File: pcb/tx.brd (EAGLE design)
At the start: 28 x 37 mm, 54 parts, among them U3 MCP73831T-2ACI/OT, Y1 CRYSTAL-26MHZSMD-3.2X2.5

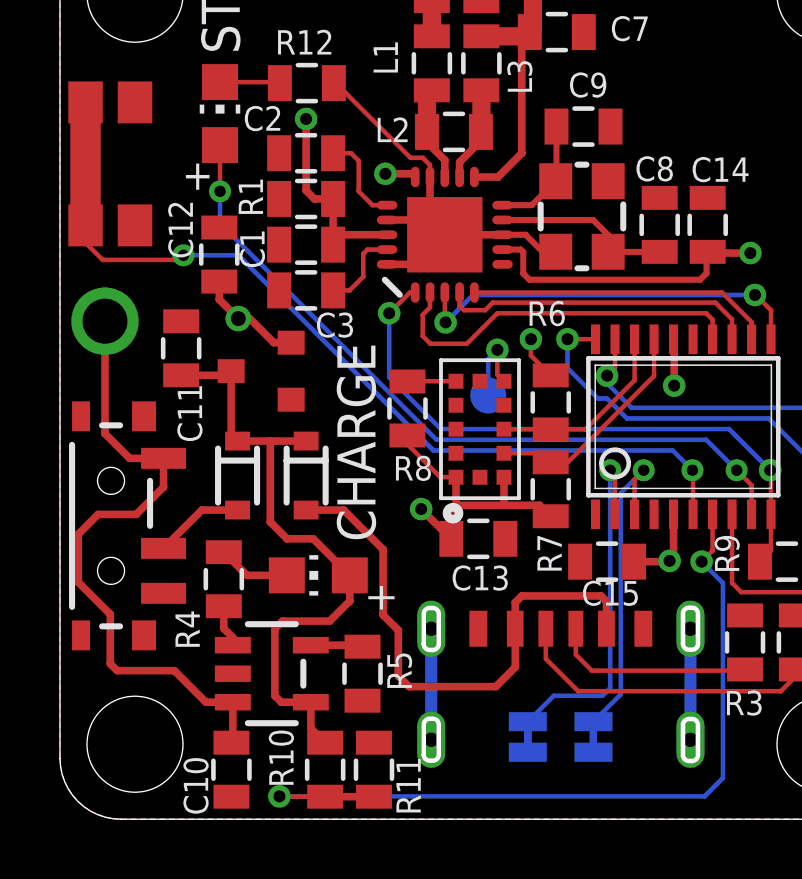
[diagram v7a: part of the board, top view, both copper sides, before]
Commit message: switched rx to tssop20
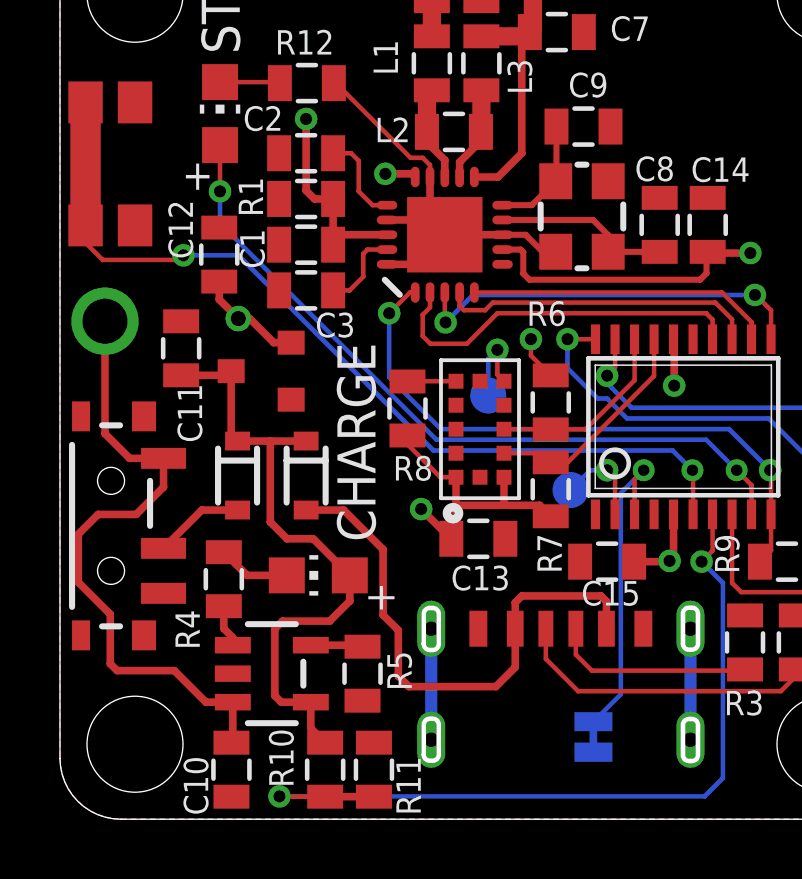
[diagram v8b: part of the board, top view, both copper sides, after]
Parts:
- removed SJ1: JUMPER-SMT_2_NC_TRACE_NO-SILK, SparkFun-Jumpers:SMT-JUMPER_2_NC_TRACE_NO-SILK
- added TP2: TPTP12R, testpad:TP12R
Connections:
- removed net N$23: SJ1.2, U$2.2
- new net N$37: TP2.TP, U$2.2
- net +3V3: no longer SJ1.1
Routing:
- net N$23: track 12.0 -> 0.00 mm, vias 1 -> 0
- net N$37: track 0.00 -> 3.07 mm, vias 0 -> 1
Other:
- board text removed: "0"
- board text removed: "1"
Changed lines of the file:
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@@
 <text x="24.765" y="15.1384" size="2.54" layer="26" rot="MR0">-</text>
 <text x="4.7244" y="29.4894" size="1.27" layer="25" rot="R270">STAT</text>
-<text x="18.161" y="3.81" size="1.27" layer="26" rot="MR0">1</text>
-<text x="15.9766" y="3.81" size="1.27" layer="26" rot="MR0">0</text>
 </plain>
 <attributes>
@@
 <attribute name="VALUE" x="29.845" y="6.096" size="1.27" layer="27" rot="R90"/>
 </element>
-<element name="SJ1" library="SparkFun-Jumpers" package="SMT-JUMPER_2_NC_TRACE_NO-SILK" value="JUMPER-SMT_2_NC_TRACE_NO-SILK" x="15.5956" y="2.7432" smashed="yes" rot="MR90">
-<attribute name="VALUE" x="14.4526" y="2.7432" size="0.6096" layer="28" font="vector" ratio="20" rot="MR90" align="top-center"/>
-</element>
 <element name="SJ2" library="SparkFun-Jumpers" package="SMT-JUMPER_2_NC_TRACE_NO-SILK" value="JUMPER-SMT_2_NC_TRACE_NO-SILK" x="17.78" y="2.7432" smashed="yes" rot="MR90">
 <attribute name="VALUE" x="16.637" y="2.7432" size="0.6096" layer="28" font="vector" ratio="20" rot="MR90" align="top-center"/>
@@
 <attribute name="TP_SIGNAL_NAME" value="" x="14.2748" y="11.5824" size="1" layer="38" rot="MR0"/>
 <attribute name="VALUE" x="14.7828" y="13.4874" size="0.0254" layer="28" rot="MR0"/>
+</element>
+<element name="TP2" library="testpad" library_urn="urn:adsk.eagle:library:385" package="TP12R" package3d_urn="urn:adsk.eagle:package:27963/1" value="TPTP12R" x="17.018" y="10.9728" smashed="yes" rot="MR0">
+<attribute name="TP_SIGNAL_NAME" value="" x="17.018" y="8.4328" size="1" layer="38" rot="MR0"/>
+<attribute name="VALUE" x="17.526" y="10.3378" size="0.0254" layer="28" rot="MR0"/>
 </element>
 </elements>
@@
 <wire x1="16.3576" y1="14.7938" x2="15.6972" y2="15.4542" width="0.1524" layer="1"/>
 <wire x1="15.6972" y1="15.4542" x2="15.6972" y2="16.002" width="0.1524" layer="1"/>
-<contactref element="SJ1" pad="1"/>
 <contactref element="SJ2" pad="1"/>
 </signal>
@@
 <wire x1="11.5918" y1="14.6" x2="11.5824" y2="14.5906" width="0.1524" layer="1"/>
 </signal>
-<signal name="N$23">
-<contactref element="U$2" pad="2"/>
-<contactref element="SJ1" pad="2"/>
-<wire x1="18.5022" y1="10.1632" x2="18.5022" y2="11.4698" width="0.1524" layer="1"/>
-<wire x1="18.5022" y1="11.4698" x2="18.3388" y2="11.6332" width="0.1524" layer="1"/>
-<via x="18.3388" y="11.6332" extent="1-16" drill="0.381"/>
-<wire x1="15.5956" y1="3.2512" x2="16.4592" y2="4.1148" width="0.1524" layer="16"/>
-<wire x1="16.4592" y1="4.1148" x2="18.0848" y2="4.1148" width="0.1524" layer="16"/>
-<wire x1="18.0848" y1="4.1148" x2="18.3388" y2="4.3688" width="0.1524" layer="16"/>
-<wire x1="18.3388" y1="4.3688" x2="18.3388" y2="11.6332" width="0.1524" layer="16"/>
-</signal>
 <signal name="N$34">
 <contactref element="SJ2" pad="2"/>
@@
 <wire x1="21.5392" y1="12.6492" x2="12.5476" y2="12.6492" width="0.1524" layer="16"/>
 <wire x1="5.334" y1="19.8628" x2="5.334" y2="20.9296" width="0.1524" layer="16"/>
-<via x="5.334" y="20.9296" extent="1-16" drill="0.381"/>
+<via x="5.334" y="20.9296" extent="1-16" drill="0.4"/>
 <wire x1="5.334" y1="20.9296" x2="5.334" y2="22.4704" width="0.1524" layer="1"/>
 <wire x1="12.5476" y1="12.6492" x2="5.334" y2="19.8628" width="0.1524" layer="16"/>
@@
 <wire x1="12.446" y1="12.2936" x2="5.9436" y2="18.796" width="0.1524" layer="16"/>
 <wire x1="5.9436" y1="18.796" x2="4.1148" y2="18.796" width="0.1524" layer="16"/>
-<via x="4.1148" y="18.796" extent="1-16" drill="0.381"/>
-<wire x1="0.8128" y1="19.7554" x2="0.8514" y2="19.794" width="0.1524" layer="1"/>
+<via x="4.1148" y="18.796" extent="1-16" drill="0.4"/>
 <wire x1="20.4216" y1="12.2936" x2="12.446" y2="12.2936" width="0.1524" layer="16"/>
 <contactref element="U$10" pad="P$3"/>
@@
 <wire x1="14.2748" y1="15.3416" x2="14.2748" y2="14.1224" width="0.1524" layer="16"/>
 </signal>
+<signal name="N$37">
+<contactref element="U$2" pad="2"/>
+<contactref element="TP2" pad="TP"/>
+<wire x1="18.5022" y1="10.1632" x2="18.5022" y2="11.3682" width="0.1524" layer="1"/>
+<wire x1="18.5022" y1="11.3682" x2="18.2372" y2="11.6332" width="0.1524" layer="1"/>
+<via x="18.2372" y="11.6332" extent="1-16" drill="0.4"/>
+<wire x1="18.2372" y1="11.6332" x2="17.6784" y2="11.6332" width="0.1524" layer="16"/>
+<wire x1="17.6784" y1="11.6332" x2="17.018" y2="10.9728" width="0.1524" layer="16"/>
+</signal>
 </signals>
